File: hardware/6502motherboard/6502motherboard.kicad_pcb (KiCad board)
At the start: 2 copper layers, 100 x 100 mm, 21 parts, among them J1 AUX 5VDC, J2 POWER 5V, J3 GND, SW1 POWER, U3 74HCT273

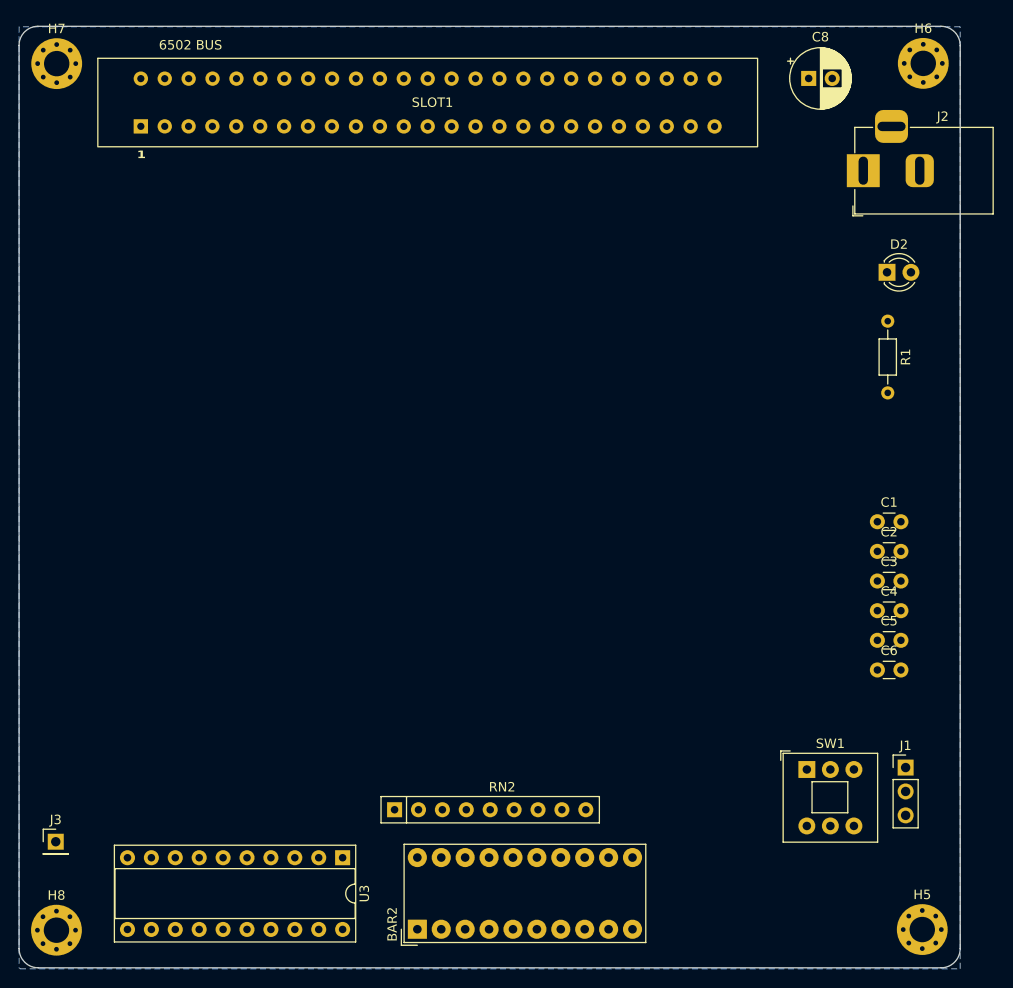
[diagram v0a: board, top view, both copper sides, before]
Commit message: Fixed 6502 Pinout, routed bus and power
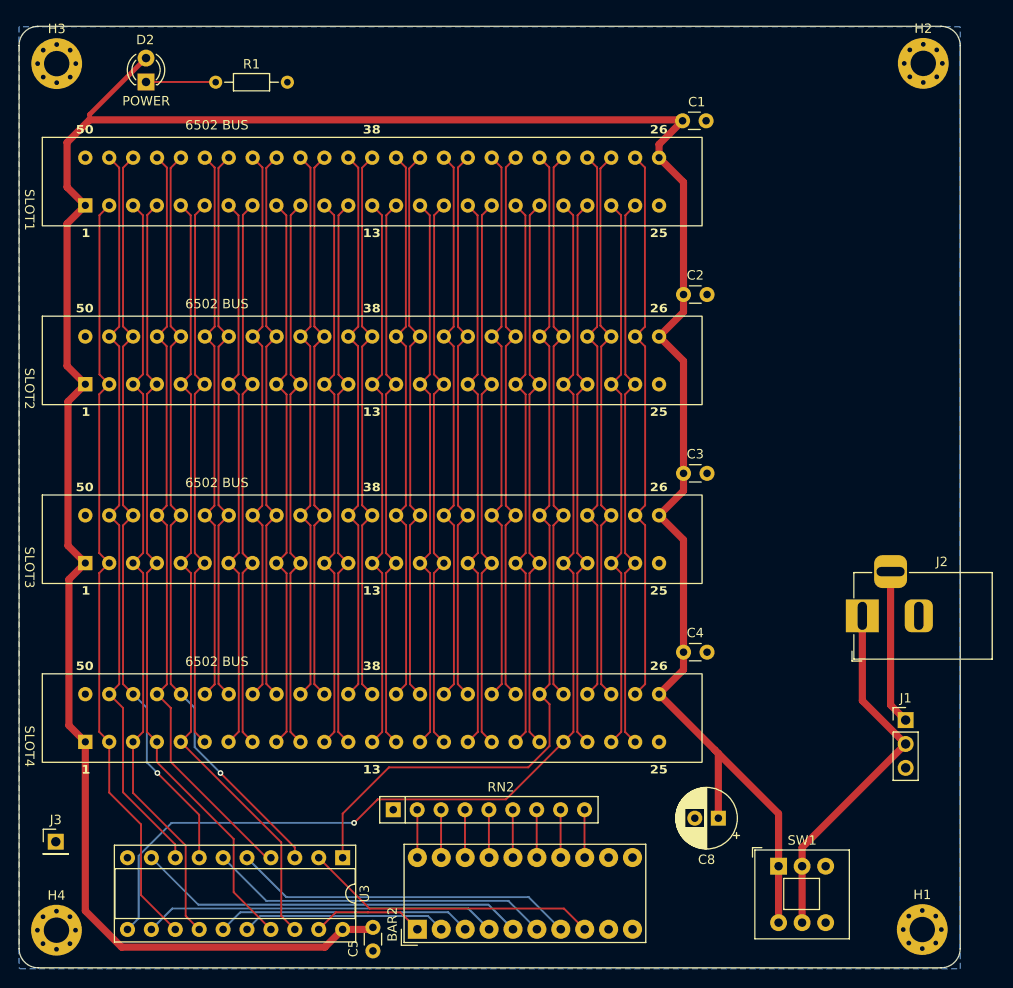
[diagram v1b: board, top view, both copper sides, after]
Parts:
- removed C6: 0.1uF, Capacitor_THT:C_Disc_D3.0mm_W1.6mm_P2.50mm
- added SLOT2: 6502 BUS, Connector_Card:EDAC 395-050-520-201, F.Cu at (122.5, 87.5)
- added SLOT3: 6502 BUS, Connector_Card:EDAC 395-050-520-201, F.Cu at (122.5, 106.5)
- added SLOT4: 6502 BUS, Connector_Card:EDAC 395-050-520-201, F.Cu at (122.5, 125.5)
- moved D2 81.3 mm to (98.5, 57.9), turned to 90 degrees
- moved C8 79.2 mm to (159.3, 136.1), turned to 180 degrees
- moved R1 75.8 mm to (105.9, 57.9), turned to 0 degrees
- moved C5 61.7 mm to (122.6, 147.7), turned to -90 degrees
- moved C1 47.4 mm to (155.5, 62.0)
- moved J2 47.3 mm to (174.6, 114.6)
- moved C2 34.2 mm to (155.6, 80.5)
- moved C3 23.6 mm to (155.6, 99.5)
- moved C4 21.1 mm to (155.6, 118.5)
- moved SW1 10.7 mm to (165.7, 141.2)
- moved SLOT1 10.3 mm to (122.5, 68.5)
- moved J1 5.05 mm to (179.2, 125.7)
- moved RN2 0.14 mm to (124.8, 135.2)
- renumbered H5 to H1, H6 to H2, H7 to H3, H8 to H4
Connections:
- SLOT1 pad 14: unconnected-(SLOT1-Pin_14-Pad14) -> NC14
- SLOT1 pad 15: unconnected-(SLOT1-Pin_15-Pad15) -> NC15
- SLOT1 pad 16: unconnected-(SLOT1-Pin_16-Pad16) -> ~{RD}
- SLOT1 pad 17: unconnected-(SLOT1-Pin_17-Pad17) -> ~{ROM_CS}
- SLOT1 pad 19: ~{ROM_CS} -> ~{NMI}
- SLOT1 pad 2: D4 -> D3
- SLOT1 pad 20: ~{NMI} -> ~{IO_CS}
- SLOT1 pad 21: ~{IO_CS} -> ~{IO_08}
- SLOT1 pad 3: D5 -> D2
- SLOT1 pad 33: ~{RAM_CS} -> NC33
- SLOT1 pad 34: ~{RD} -> NC34
- SLOT1 pad 36: unconnected-(SLOT1-Pin_36-Pad36) -> ~{RAM_CS}
- SLOT1 pad 37: unconnected-(SLOT1-Pin_37-Pad37) -> NC37
- SLOT1 pad 4: D6 -> D1
- SLOT1 pad 46: D0 -> D7
- SLOT1 pad 47: D1 -> D6
- SLOT1 pad 48: D2 -> D5
- SLOT1 pad 49: D3 -> D4
- SLOT1 pad 5: D7 -> D0
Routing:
- net VCC: track 0.00 -> 300.9 mm
- net ~{IO_08}: track 0.00 -> 118.1 mm, vias 0 -> 1
- net ~{RESET}: track 0.00 -> 95.2 mm
- net D0: track 0.00 -> 84.6 mm
- net D1: track 0.00 -> 84.5 mm
- net D2: track 0.00 -> 82.5 mm
- net D3: track 0.00 -> 82.5 mm
- net D6: track 0.00 -> 82.2 mm
- net D7: track 0.00 -> 82.1 mm, vias 0 -> 1
- net D5: track 0.00 -> 80.0 mm, vias 0 -> 1
- net D4: track 0.00 -> 79.9 mm
- net ~{IO_03}: track 0.00 -> 59.7 mm
- net A12: track 0.00 -> 59.7 mm
- net A14: track 0.00 -> 59.7 mm
- net ~{RAM_CS}: track 0.00 -> 59.7 mm
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
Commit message: v1.0 Motherboard Ready
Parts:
- added SW2: SW_Push, Button_Switch_THT:SW_PUSH_6mm_H5mm, F.Cu at (162.7, 142.2)
- added T1: DS-1813, Package_TO_SOT_THT:21-0248A_MAXIM, F.Cu at (151.9, 135.4)
- moved J1 27.4 mm to (172.6, 99.1), turned to 90 degrees
- moved SW1 14.8 mm to (175.1, 129.8)
- moved C8 12.0 mm to (162.8, 124.6), turned to 0 degrees
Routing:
- net ~{RESET}: track 95.2 -> 134.2 mm, vias 0 -> 1
- net VCC: track 300.9 -> 310.4 mm
- net /AUX GND: track 16.4 -> 18.4 mm
- net /5VDC IN: track 39.1 -> 38.2 mm
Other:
- board text added: "RESET"

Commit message: v1.6 Motherboard Complete
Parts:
- removed D2: POWER, LED_THT:LED_D3.0mm
- removed R1: 220, Resistor_THT:R_Axial_DIN0204_L3.6mm_D1.6mm_P7.62mm_Horizontal
- added R2: 220, Resistor_THT:R_Axial_DIN0204_L3.6mm_D1.6mm_P7.62mm_Horizontal, F.Cu at (155.8, 147.9)
- added SLOT5: 6502 BUS, Connector_PinHeader_2.54mm:PinHeader_2x25_P2.54mm_Vertical_Counter_Clockwise, F.Cu at (104.5, 56.6)
- moved C1 6.40 mm to (160.5, 66.0), turned to -90 degrees
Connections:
- BAR2 pad 10: unconnected-(BAR2-A-Pad10) -> Net-(BAR2-A-Pad10)
- BAR2 pad 11: unconnected-(BAR2-K-Pad11) -> VCC
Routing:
- net VCC: track 310.4 -> 342.4 mm
- net D3: track 82.5 -> 104.7 mm
- net D7: track 82.1 -> 103.9 mm
- net ~{RD}: track 59.6 -> 81.3 mm
- net A3: track 59.7 -> 81.1 mm
- net D2: track 82.5 -> 103.9 mm
- net A4: track 59.6 -> 81.0 mm
- net A5: track 59.6 -> 80.8 mm
- net NC14: track 59.6 -> 80.7 mm
- net A6: track 59.6 -> 80.7 mm
- net A7: track 59.6 -> 80.5 mm
- net A1: track 59.7 -> 80.5 mm
- net D1: track 84.5 -> 105.3 mm
- net ~{IO_04}: track 59.6 -> 80.4 mm
- net ~{IO_06}: track 59.6 -> 80.4 mm
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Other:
- board text added: "(C) Mariano Luna"
- board text added: "V1.6"
- board text added: "simple6502 Motherboard"

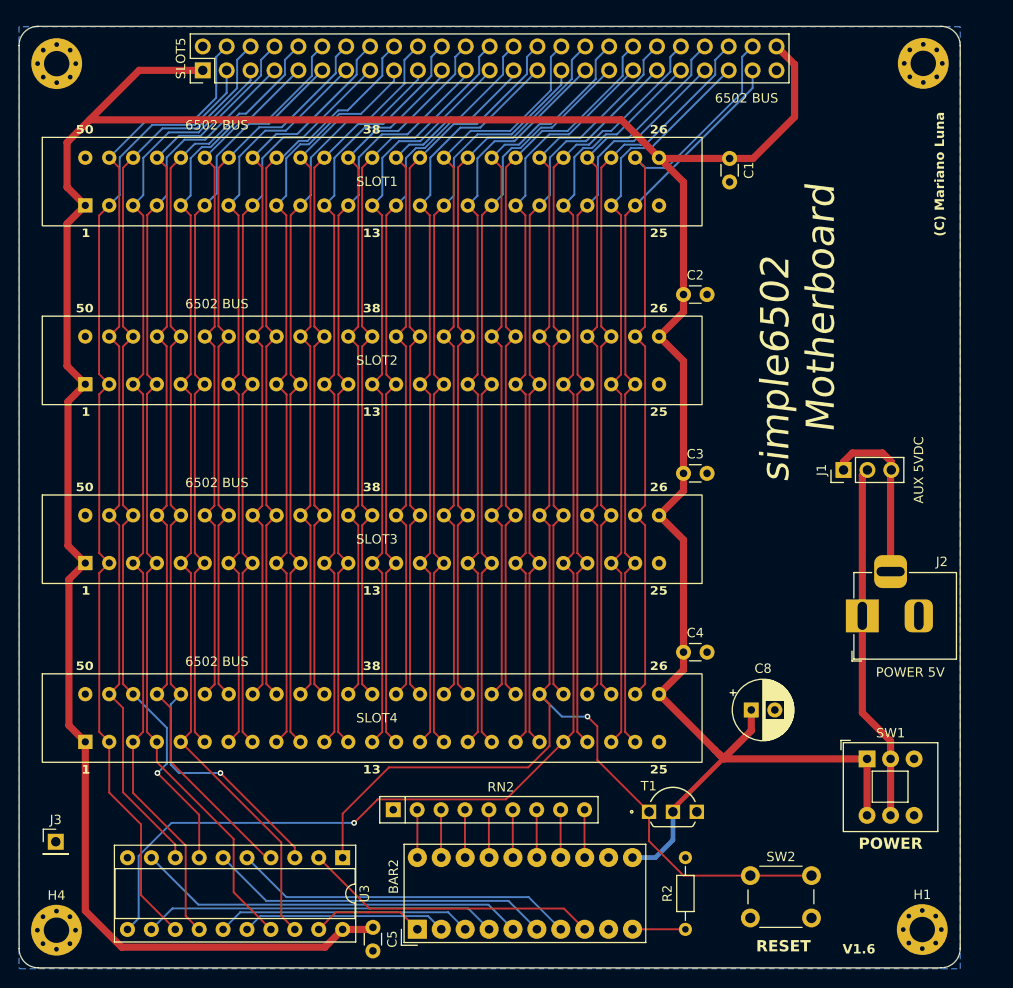
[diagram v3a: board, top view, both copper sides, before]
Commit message: Motherboard added 7805 regulator
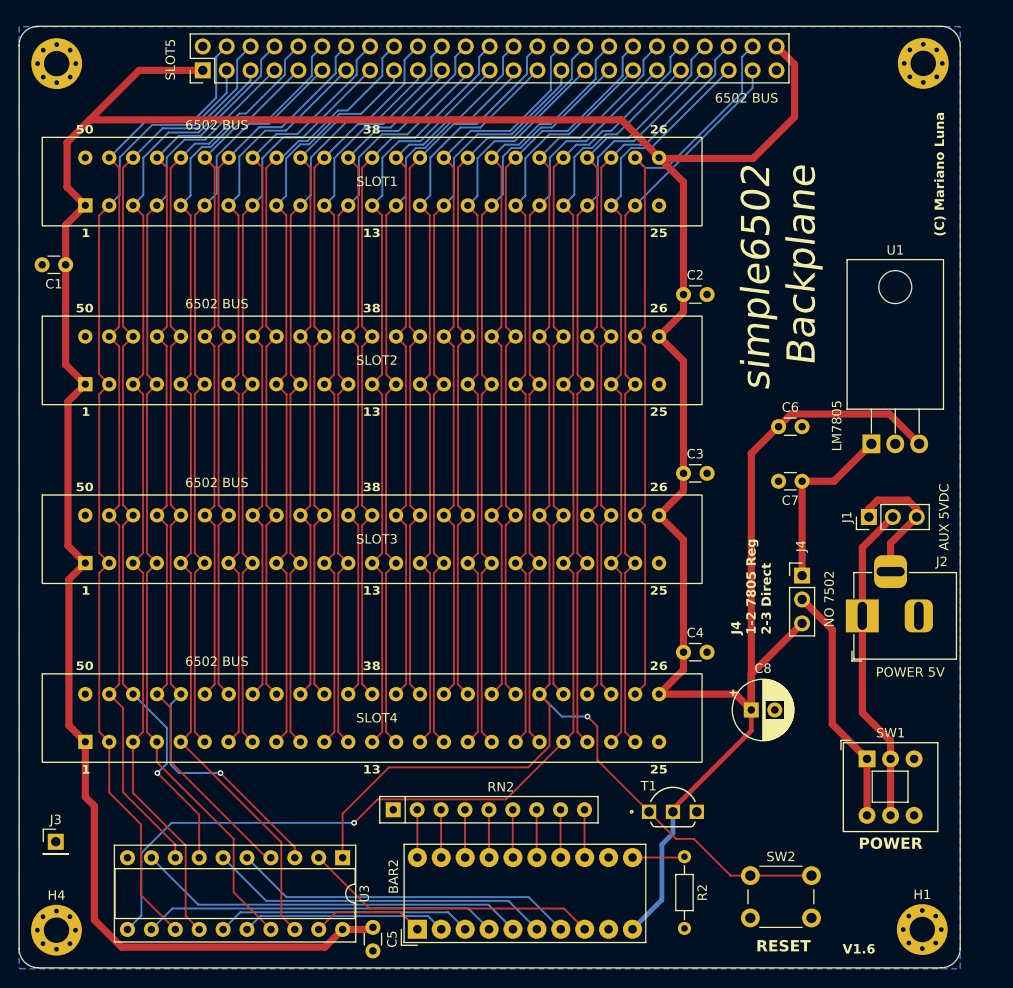
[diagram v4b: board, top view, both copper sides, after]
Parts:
- added C6: 100nF, Capacitor_THT:C_Disc_D3.0mm_W1.6mm_P2.50mm, F.Cu at (165.7, 94.5)
- added C7: 330nF, Capacitor_THT:C_Disc_D3.0mm_W1.6mm_P2.50mm, F.Cu at (168.2, 100.3)
- added J4: NO 7502, Connector_PinHeader_2.54mm:PinHeader_1x03_P2.54mm_Vertical, F.Cu at (168.2, 110.3)
- added U1: LM7805, Package_TO_SOT_THT:TO-220-3_Horizontal_TabDown, F.Cu at (175.6, 96.3)
- C8: value 1000uF -> 10uF
- moved C1 71.4 mm to (90.0, 77.3), turned to 180 degrees
- moved R2 7.72 mm to (155.7, 140.2), turned to -90 degrees
- moved J1 5.68 mm to (175.3, 104.1)
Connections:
- net /5VDC IN renamed /VDC
- BAR2 pad 10: Net-(BAR2-A-Pad10) -> VCC
- BAR2 pad 11: VCC -> Net-(BAR2-K-Pad11)
- R2 pad 1: Net-(BAR2-A-Pad10) -> Net-(BAR2-K-Pad11)
- SW1 pad 1: VCC -> VDC_IN
- SW1 pad 4: VCC -> VDC_IN
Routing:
- net VCC: track 342.4 -> 385.7 mm
- net VDC_IN: track 0.00 -> 25.8 mm
- net /V_IN: track 0.00 -> 19.0 mm
- net Net-(BAR2-A-Pad10): track 5.62 -> 0.00 mm
- net Net-(BAR2-K-Pad11): track 0.00 -> 5.56 mm
- net /AUX GND: track 18.4 -> 14.5 mm
- net /VDC: track 38.2 -> 34.3 mm
- net ~{RESET}: track 154.3 -> 152.5 mm
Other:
- board text added: "J4 1-2 7805 Reg 2-3 Direct"
- board text added: "simple6502 Backplane"
- board text removed: "simple6502 Motherboard"

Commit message: I_O8 Jumper and more PCB cleanup
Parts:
- added J5: IO_8, Connector_PinHeader_2.54mm:PinHeader_1x02_P2.54mm_Vertical, F.Cu at (115.5, 135.8)
- SLOT 5: renamed from SLOT5
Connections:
- U3 pad 11: ~{IO_08} -> /~{U3_CS}
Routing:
- net ~{IO_08}: track 138.8 -> 108.5 mm, vias 1 -> 0
- net /~{U3_CS}: track 0.00 -> 27.8 mm
- net ~{RESET}: track 152.5 -> 157.5 mm
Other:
- board text added: "1"
- board text added: "25"

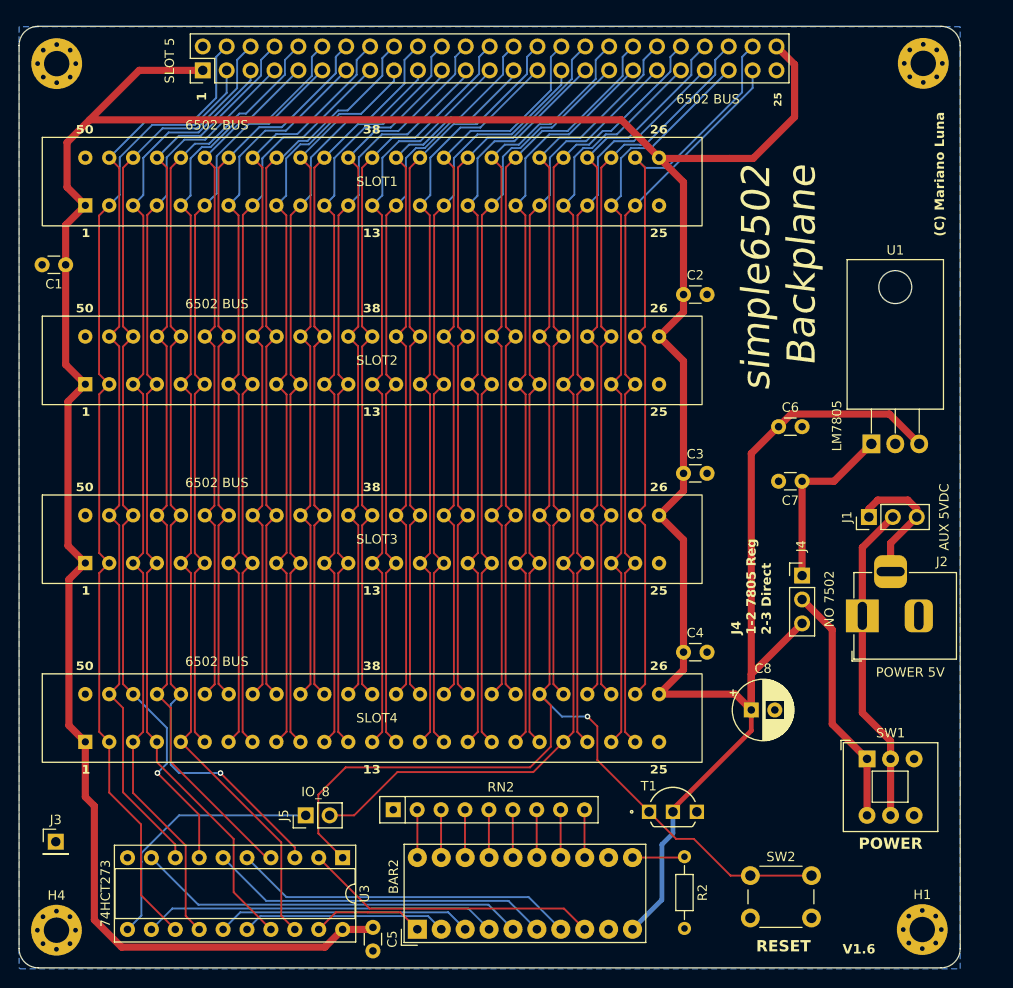
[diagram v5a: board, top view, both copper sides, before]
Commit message: rev 1.8 new pcb optimized power routing
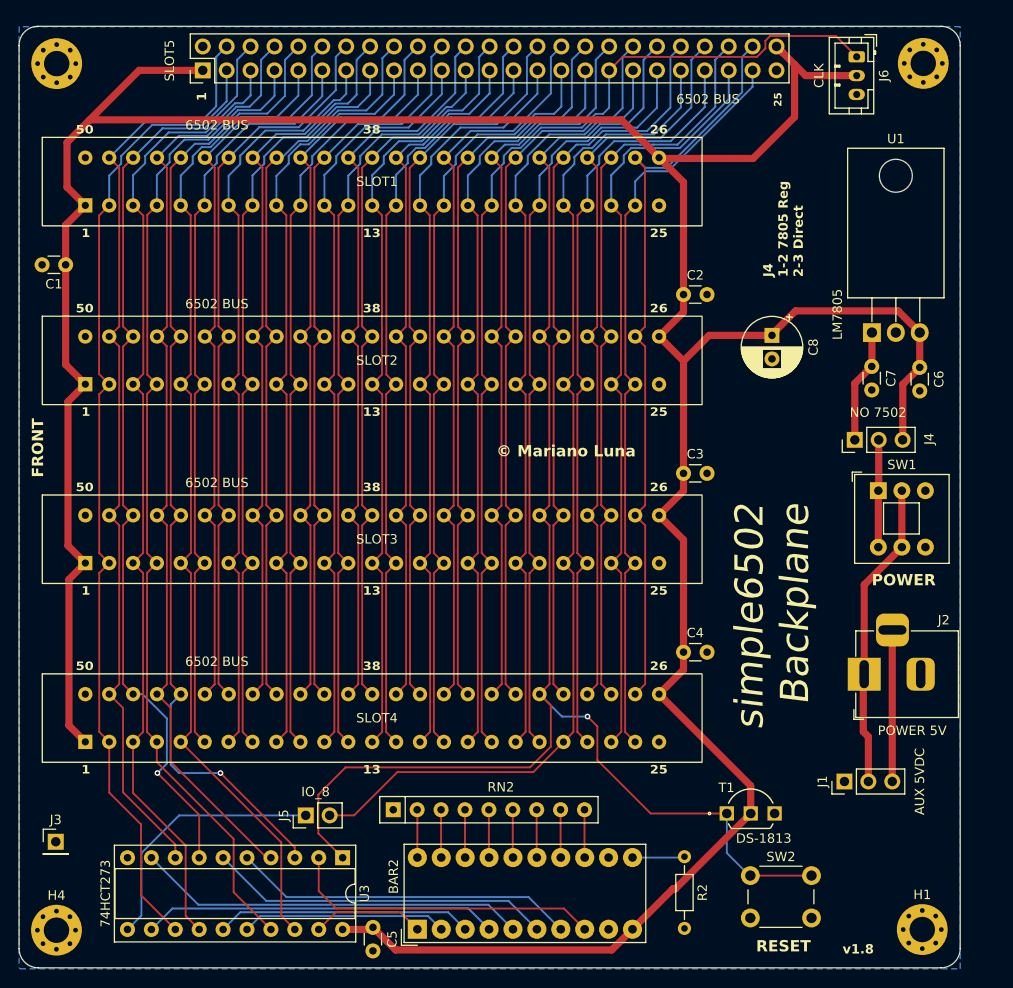
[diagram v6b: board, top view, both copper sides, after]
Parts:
- added J6: CLK, Connector_JST:JST_PH_B3B-PH-K_1x03_P2.00mm_Vertical, F.Cu at (174.0, 55.2)
- SLOT5: renamed from SLOT 5
- moved C8 39.9 mm to (165.0, 84.8), turned to -90 degrees
- moved SW1 28.5 mm to (176.3, 101.3)
- moved J1 28.2 mm to (172.7, 132.2)
- moved C6 16.3 mm to (180.7, 88.2), turned to -90 degrees
- moved J4 15.5 mm to (173.8, 95.9), turned to 90 degrees
- moved C7 14.3 mm to (175.6, 88.1), turned to -90 degrees
- moved U1 11.8 mm to (175.6, 84.5)
- moved T1 8.27 mm to (160.2, 135.6)
- moved J2 6.20 mm to (174.8, 120.8)
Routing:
- net VCC: track 385.7 -> 351.7 mm
- net CLK: track 80.4 -> 111.9 mm
- net VDC_IN: track 25.8 -> 11.4 mm
- net /V_IN: track 19.0 -> 12.2 mm
- net ~{RESET}: track 157.5 -> 162.1 mm
- net ~{NMI}: track 80.4 -> 82.7 mm
- net ~{ROM_CS}: track 80.4 -> 82.7 mm
- net ~{IO_CS}: track 80.4 -> 82.7 mm
- net ~{IO_08}: track 108.5 -> 110.8 mm
- net ~{IO_06}: track 80.4 -> 82.7 mm
- net ~{IO_07}: track 77.9 -> 80.1 mm
- net /L7: track 31.4 -> 33.5 mm
- net ~{IO_03}: track 77.9 -> 79.9 mm
- net ~{IO_05}: track 77.9 -> 80.0 mm
- net ~{IRQ}: track 78.2 -> 80.2 mm
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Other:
- board text added: "FRONT"
- board text added: "v${REVISION}"
- board text added: "© ${COMPANY}"
- board text removed: "(C) Mariano Luna"
- board text removed: "V1.6"

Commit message: rev 1.8.1 pcb routed external connector in top layer
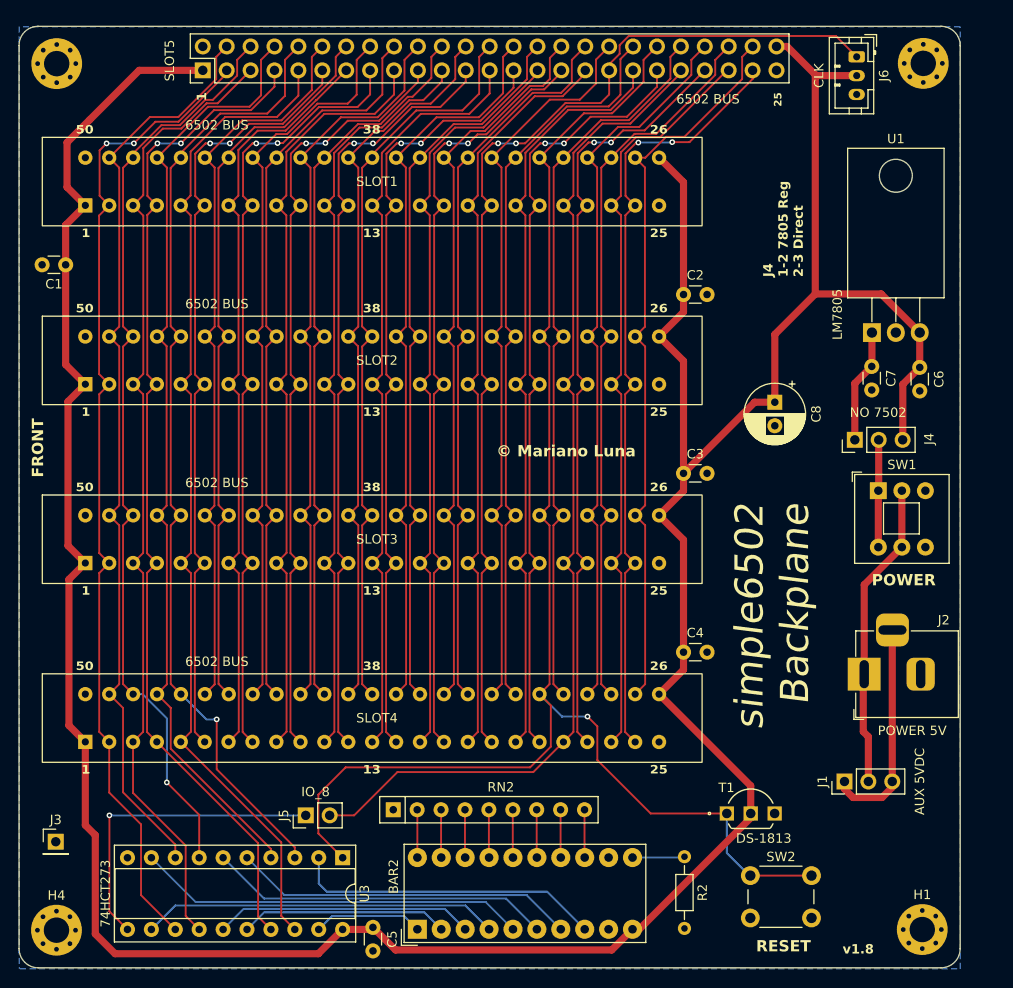
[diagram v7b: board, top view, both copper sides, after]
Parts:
- moved C8 7.11 mm to (165.3, 91.9)
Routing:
- net /AUX GND: track 16.1 -> 23.4 mm
- net /~{U3_CS}: track 27.8 -> 33.8 mm, vias 0 -> 1
- net ~{IO_02}: track 80.6 -> 83.3 mm, vias 0 -> 2
- net D7: track 105.2 -> 102.7 mm
- net A2: track 81.8 -> 84.2 mm, vias 0 -> 2
- net NC14: track 81.8 -> 83.8 mm, vias 0 -> 2
- net ~{IO_05}: track 80.0 -> 77.9 mm
- net ~{IO_03}: track 79.9 -> 78.0 mm
- net CLK: track 111.9 -> 113.9 mm, vias 0 -> 2
- net ~{ROM_CS}: track 82.7 -> 80.9 mm
- net ~{IO_08}: track 110.8 -> 108.9 mm
- net D5: track 101.0 -> 99.2 mm
- net ~{IO_07}: track 80.1 -> 78.3 mm
- net D1: track 106.9 -> 108.6 mm, vias 0 -> 2
- net ~{IO_01}: track 80.1 -> 78.4 mm
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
